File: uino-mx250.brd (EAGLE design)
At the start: 68.6 x 53.3 mm, 32 parts, among them J1 CON_TERMINAL_BLOCK_02-5MM, U1 L4931, U2 PIC32MX250B-P

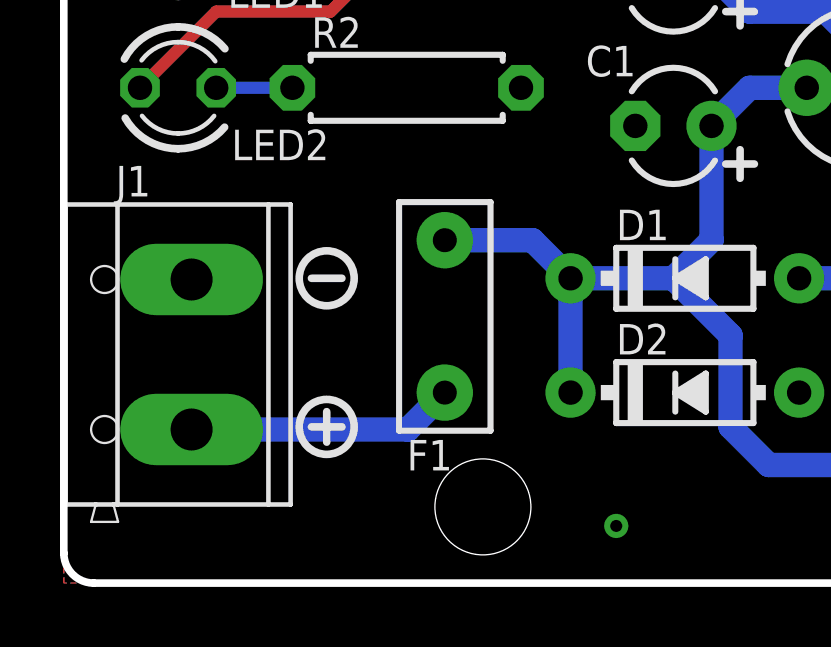
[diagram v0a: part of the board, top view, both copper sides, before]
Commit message: Adjusted power input layout.
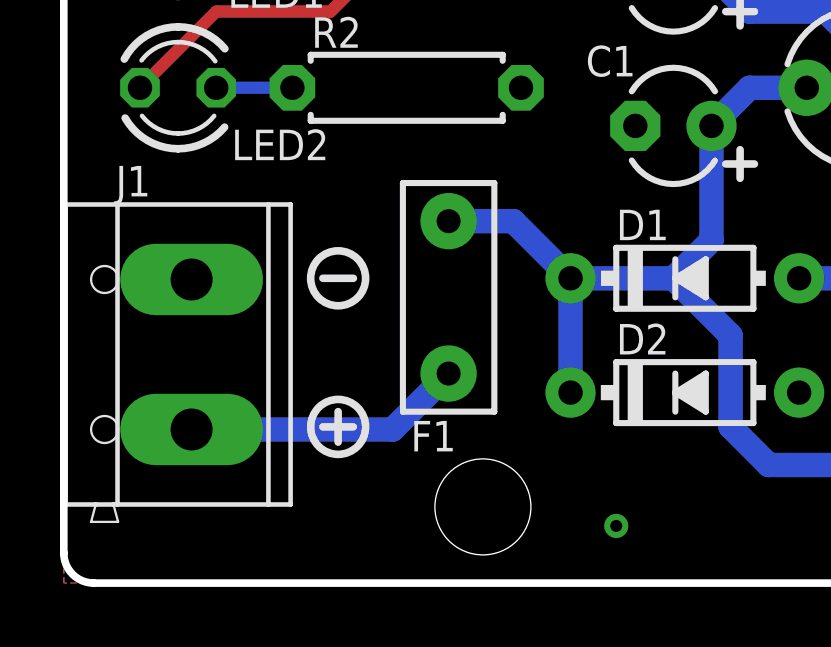
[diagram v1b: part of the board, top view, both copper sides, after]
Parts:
- moved F1 0.65 mm to (12.8, 9.53)
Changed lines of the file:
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@@
 <text x="56.007" y="39.624" size="1.6764" layer="22" font="vector" ratio="18" rot="MR0">Designed with &lt;3
 for Mathew Linden</text>
-<circle x="8.763" y="10.16" radius="0.915809375" width="0.254" layer="21"/>
-<wire x1="8.255" y1="10.16" x2="9.271" y2="10.16" width="0.254" layer="21"/>
-<circle x="8.763" y="5.207" radius="0.915809375" width="0.254" layer="21"/>
-<wire x1="8.255" y1="5.207" x2="9.271" y2="5.207" width="0.254" layer="21"/>
-<wire x1="8.763" y1="4.699" x2="8.763" y2="5.715" width="0.254" layer="21"/>
+<circle x="9.144" y="10.16" radius="0.915809375" width="0.254" layer="21"/>
+<wire x1="8.636" y1="10.16" x2="9.652" y2="10.16" width="0.254" layer="21"/>
+<circle x="9.144" y="5.207" radius="0.915809375" width="0.254" layer="21"/>
+<wire x1="8.636" y1="5.207" x2="9.652" y2="5.207" width="0.254" layer="21"/>
+<wire x1="9.144" y1="4.699" x2="9.144" y2="5.715" width="0.254" layer="21"/>
 </plain>
 <attributes>
@@
 <attribute name="VALUE" x="27.94" y="19.685" size="0.4064" layer="27" ratio="10" rot="R90"/>
 </element>
-<element name="F1" library="adi-misc" package="PTC" value="" x="12.7" y="8.89" smashed="yes" rot="R90">
-<attribute name="NAME" x="12.954" y="4.772" size="1.016" layer="25" ratio="18" rot="R180"/>
-<attribute name="VALUE" x="14.84" y="5.08" size="0.4318" layer="27" rot="R90"/>
+<element name="F1" library="adi-misc" package="PTC" value="" x="12.827" y="9.525" smashed="yes" rot="R90">
+<attribute name="NAME" x="13.081" y="5.407" size="1.016" layer="25" ratio="18" rot="R180"/>
+<attribute name="VALUE" x="14.967" y="5.715" size="0.4318" layer="27" rot="R90"/>
 </element>
 <element name="F2" library="adi-misc" package="PTC" value="" x="16.51" y="36.83" smashed="yes">
@@
 <wire x1="44.45" y1="5.715" x2="30.607" y2="5.715" width="0.8128" layer="16"/>
 <wire x1="22.225" y1="8.255" x2="20.32" y2="10.16" width="0.8128" layer="16"/>
-<wire x1="16.891" y1="10.16" x2="15.621" y2="11.43" width="0.8128" layer="16"/>
-<wire x1="15.621" y1="11.43" x2="12.7" y2="11.43" width="0.8128" layer="16"/>
 <wire x1="22.225" y1="8.255" x2="22.225" y2="5.207" width="0.8128" layer="16"/>
 <wire x1="22.225" y1="5.207" x2="23.495" y2="3.937" width="0.8128" layer="16"/>
@@
 <wire x1="21.59" y1="15.24" x2="22.86" y2="16.51" width="0.8128" layer="16"/>
 <wire x1="22.86" y1="16.51" x2="24.765" y2="16.51" width="0.8128" layer="16"/>
+<wire x1="12.827" y1="12.065" x2="14.986" y2="12.065" width="0.8128" layer="16"/>
+<wire x1="14.986" y1="12.065" x2="16.891" y2="10.16" width="0.8128" layer="16"/>
 </signal>
 <signal name="GND">
@@
 <contactref element="J1" pad="2"/>
 <contactref element="F1" pad="P$1"/>
-<wire x1="4.26" y1="5.12" x2="11.47" y2="5.12" width="0.8128" layer="16"/>
-<wire x1="11.47" y1="5.12" x2="12.7" y2="6.35" width="0.8128" layer="16"/>
+<wire x1="4.26" y1="5.12" x2="10.962" y2="5.12" width="0.8128" layer="16"/>
+<wire x1="10.962" y1="5.12" x2="12.827" y2="6.985" width="0.8128" layer="16"/>
 </signal>
 </signals>
